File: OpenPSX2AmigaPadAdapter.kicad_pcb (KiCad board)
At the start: 2 copper layers, 58.9 x 44.2 mm, 43 parts, among them J1 TO_PSX_PAD, J2 DB9_F, J3 CONN_FTDI, J4 CONN_ICSP, J99 OSHW_LOGO, Q1 BSS138, Q2 BSS138, Q3 BSS138, Q4 BSS138, Q5 BSS138, U1 ATmega328P-AU, U2 LM1117-3.3, Y1 16M, Y2 16M

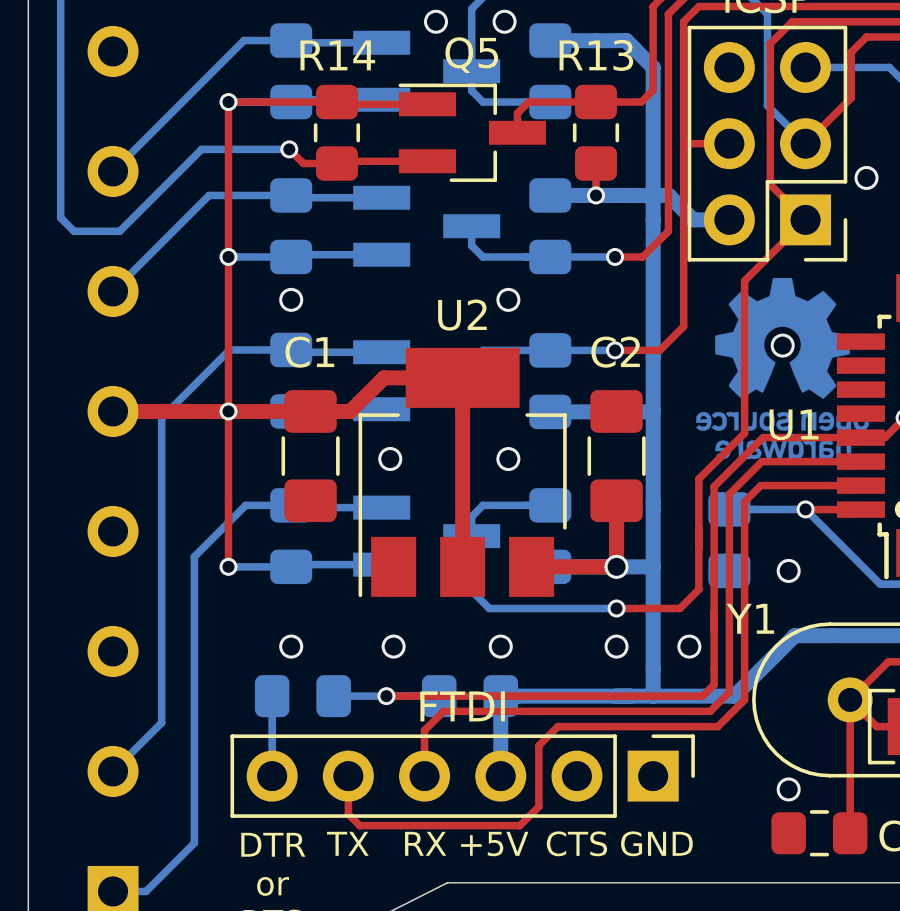
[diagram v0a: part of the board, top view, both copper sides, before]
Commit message: Update schematics for analog output support. PCB TBD.
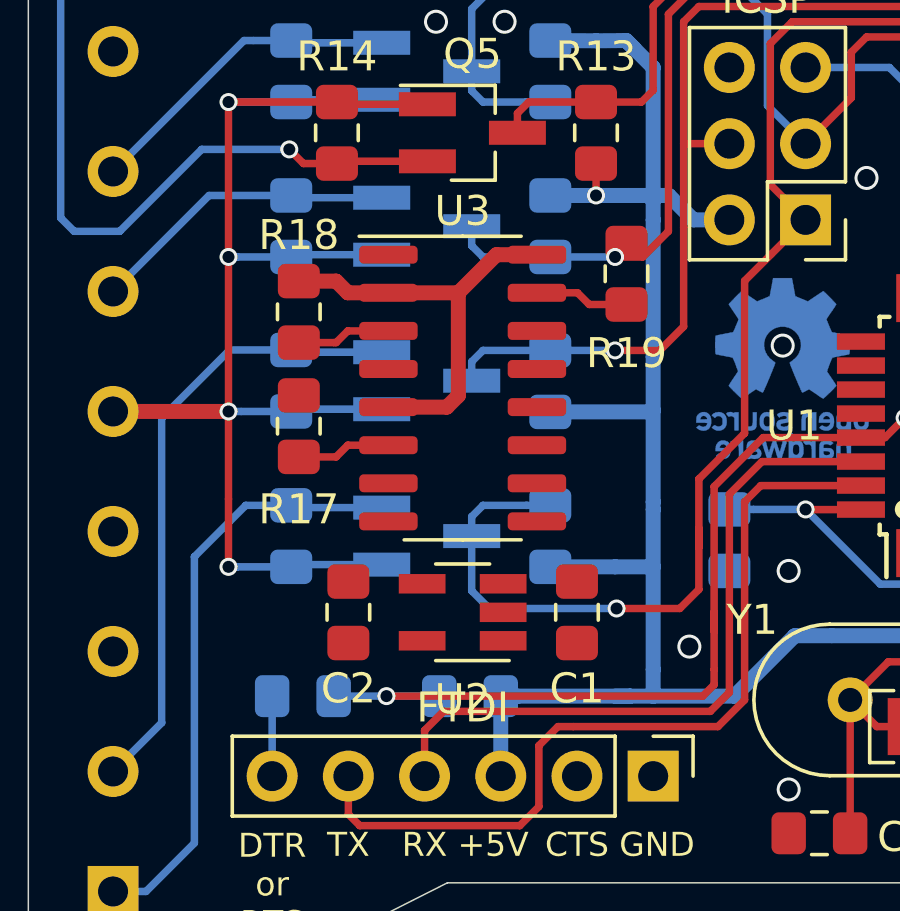
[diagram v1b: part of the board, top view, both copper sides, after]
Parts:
- added R17: 10k, Resistor_SMD:R_0805_2012Metric_Pad1.15x1.40mm_HandSolder, F.Cu at (122.8, 76.5)
- added R18: 1M, Resistor_SMD:R_0805_2012Metric_Pad1.15x1.40mm_HandSolder, F.Cu at (122.8, 72.7)
- added R19: 1M, Resistor_SMD:R_0805_2012Metric_Pad1.15x1.40mm_HandSolder, F.Cu at (133.7, 71.4)
- added U3: AD5242, Package_SO:SOIC-16_3.9x9.9mm_P1.27mm, F.Cu at (128.3, 75.2)
- C1, C2: value 10u -> 1u; footprint Capacitor_SMD:C_1206_3216Metric_Pad1.42x1.75mm_HandSolder -> Capacitor_SMD:C_0805_2012Metric_Pad1.15x1.40mm_HandSolder
- U2: value LM1117-3.3 -> TC1185-3.3V; footprint Package_TO_SOT_SMD:SOT-223-3_TabPin2 -> Package_TO_SOT_SMD:SOT-23-5_HandSoldering
- moved C2 10.3 mm to (124.5, 82.7), turned to 90 degrees
- moved C1 10.3 mm to (132.1, 82.7)
- moved U2 4.67 mm to (128.3, 82.7), turned to 180 degrees
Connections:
- C1 pad 1: GND -> +5V
- C1 pad 2: +3V3 -> GND
- C2 pad 1: GND -> +3V3
- C2 pad 2: +5V -> GND
- U1 pad 27: (no net) -> /sda
- U1 pad 28: (no net) -> /scl
- U2 pad 1: GND -> +5V
- U2 pad 2: +3V3 -> GND
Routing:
- net +3V3: track 61.2 -> 46.7 mm
- net +5V: track 106.1 -> 115.6 mm, vias 6 -> 5
- net Net-(R17-Pad1): track 0.00 -> 3.15 mm
- net /ami_potx: track 23.2 -> 26.3 mm
- net /ami_poty: track 18.2 -> 21.4 mm
- net GND: vias 42 -> 34

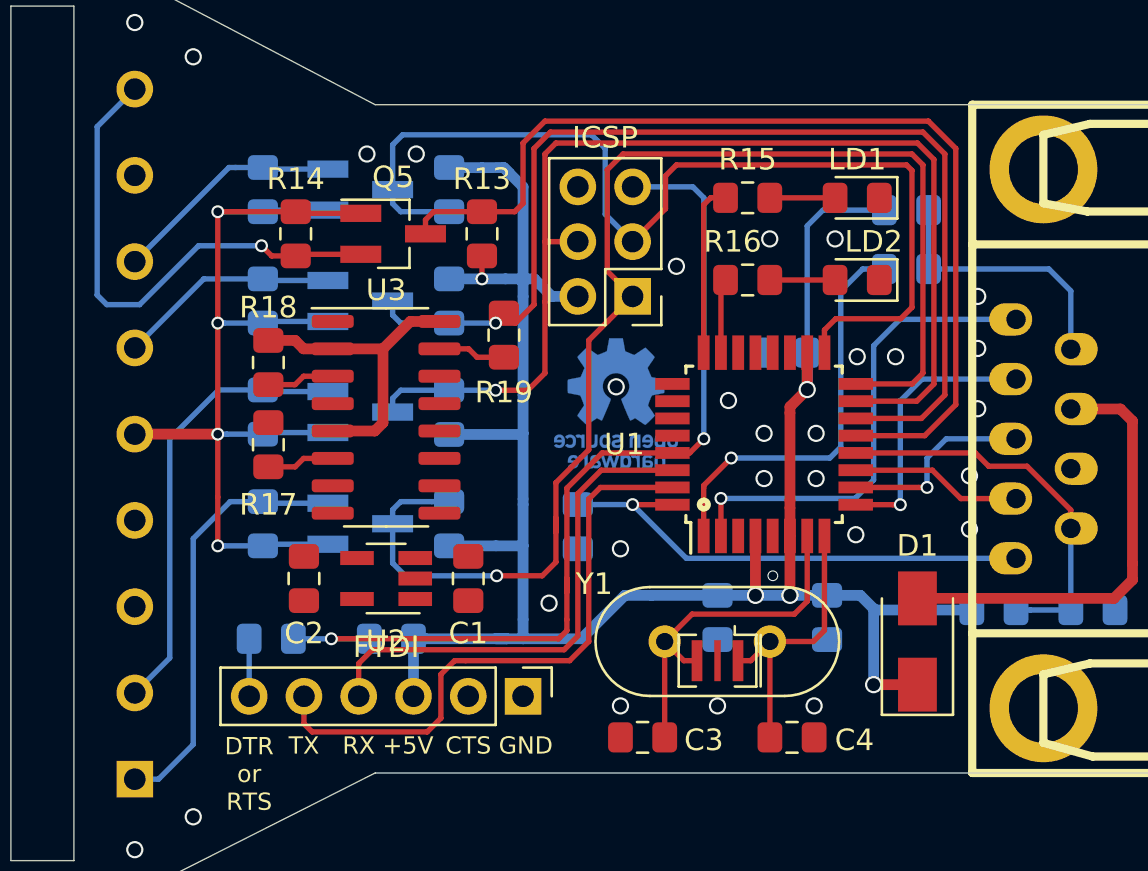
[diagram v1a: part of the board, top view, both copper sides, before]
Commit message: PCB modifications for analog support are complete
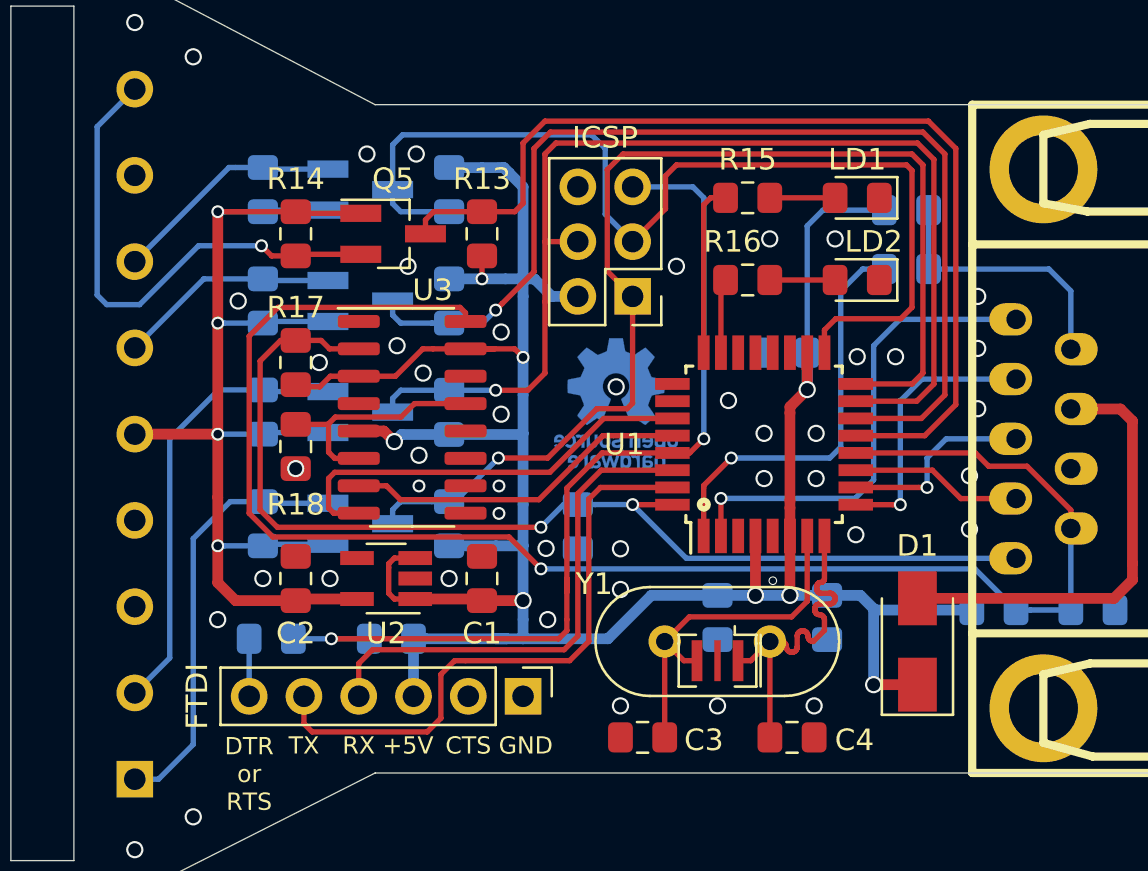
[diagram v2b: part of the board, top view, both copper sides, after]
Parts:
- removed R19: 1M, Resistor_SMD:R_0805_2012Metric_Pad1.15x1.40mm_HandSolder
- moved R18 1.27 mm to (124.1, 76.6), turned to 270 degrees
- moved R17 1.27 mm to (124.1, 72.7), turned to 270 degrees
- moved U3 1.21 mm to (129.5, 75.2)
- moved C1 0.63 mm to (132.7, 82.7)
- moved C2 0.38 mm to (124.1, 82.7)
- renumbered R18 to R17, R17 to R18
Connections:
- net Net-(C3-Pad2) renamed /clk-
- net Net-(C4-Pad2) renamed /clk+
- R18 pad 1: Net-(R17-Pad1) -> Net-(R18-Pad1)
- U3 pad 1: Net-(R17-Pad1) -> (no net)
- U3 pad 13: (no net) -> Net-(R18-Pad1)
- U3 pad 15: /ami_poty -> +5V
- U3 pad 16: +5V -> /ami_poty
- U3 pad 2: +5V -> /ami_potx
- U3 pad 3: /ami_potx -> +5V
- U3 pad 6: Net-(R17-Pad1) -> Net-(R18-Pad1)
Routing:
- net /ami_poty: track 21.4 -> 75.0 mm, vias 0 -> 1
- net /ami_potx: track 26.3 -> 50.7 mm, vias 1 -> 2
- net /sda: track 0.00 -> 20.0 mm
- net /scl: track 0.00 -> 16.0 mm
- net +5V: track 115.6 -> 127.6 mm, vias 5 -> 8
- net Net-(R18-Pad1): track 0.00 -> 11.1 mm
- net /miso: track 62.2 -> 53.3 mm
- net +3V3: track 46.7 -> 55.2 mm
- net /clk+: track 13.3 -> 16.5 mm
- net Net-(R17-Pad1): track 3.15 -> 0.00 mm
- net /ps_attn: track 50.5 -> 49.6 mm
- net GND: vias 34 -> 52

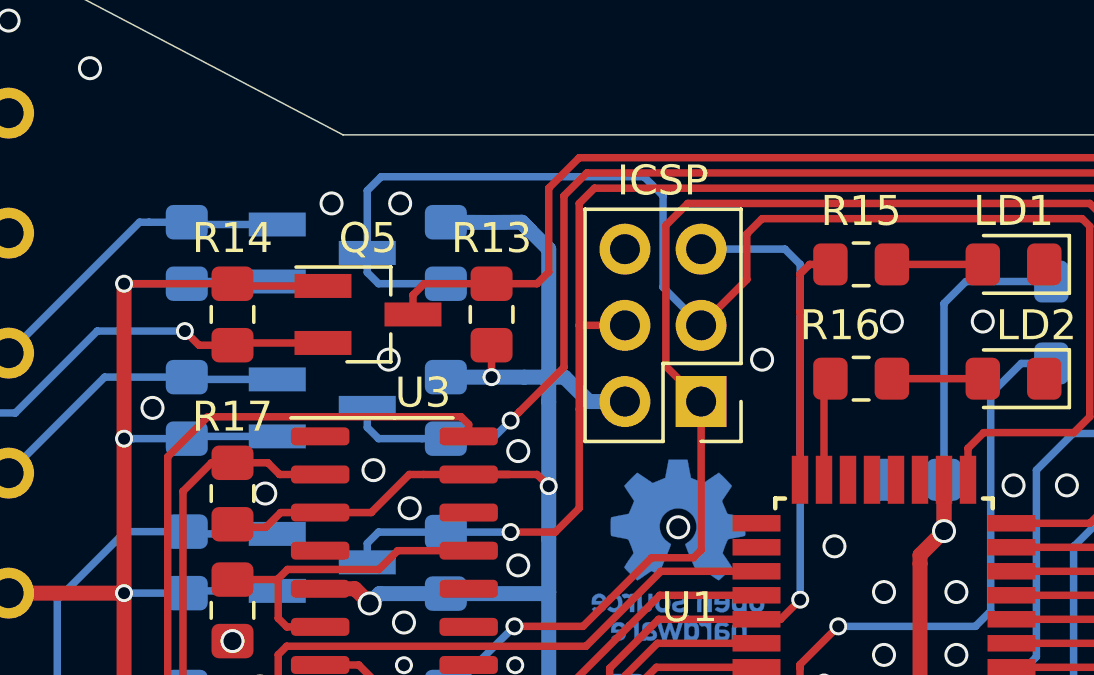
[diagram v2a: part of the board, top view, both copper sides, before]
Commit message: Fix component naming
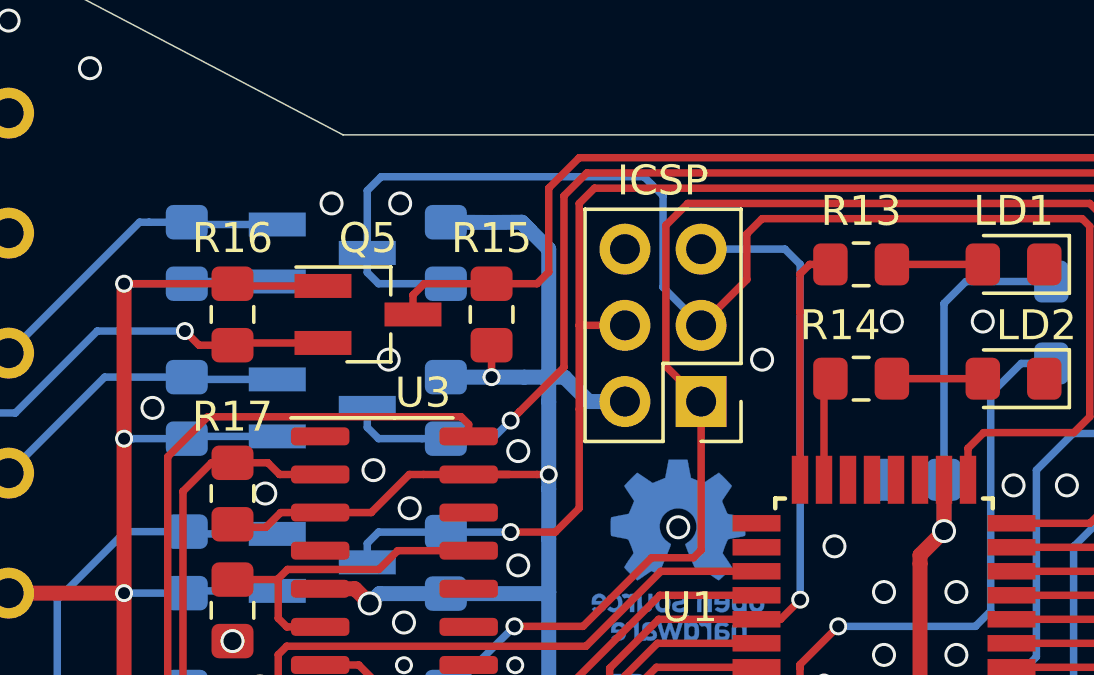
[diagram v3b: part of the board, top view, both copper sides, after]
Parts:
- renumbered R15 to R13, R16 to R14, R13 to R15, R14 to R16
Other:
- board text added: "V4"
- board text removed: "V3"
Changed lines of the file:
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@@
     (0 F.Cu signal)
     (31 B.Cu signal)
-    (36 B.SilkS user hide)
+    (36 B.SilkS user)
     (37 F.SilkS user)
     (38 B.Mask user)
@@
     (tags "resistor handsolder")
     (attr smd)
-    (fp_text reference R16 (at 0.6985 1.778) (layer F.SilkS)
+    (fp_text reference R14 (at 0.6985 1.778) (layer F.SilkS)
       (effects (font (size 1 1) (thickness 0.15)))
     )
@@
     (tags "resistor handsolder")
     (attr smd)
-    (fp_text reference R15 (at 0 1.778) (layer F.SilkS)
+    (fp_text reference R13 (at 0 1.778) (layer F.SilkS)
       (effects (font (size 1 1) (thickness 0.15)))
     )
@@
     (tags "resistor handsolder")
     (attr smd)
-    (fp_text reference R13 (at 2.542999 0 180) (layer F.SilkS)
+    (fp_text reference R15 (at 2.542999 0 180) (layer F.SilkS)
       (effects (font (size 1 1) (thickness 0.15)))
     )
@@
     (tags "resistor handsolder")
     (attr smd)
-    (fp_text reference R14 (at -2.542999 0 180) (layer F.SilkS)
+    (fp_text reference R16 (at -2.542999 0 180) (layer F.SilkS)
       (effects (font (size 1 1) (thickness 0.15)))
     )
@@
     (effects (font (size 1 1) (thickness 0.15)) (justify mirror))
   )
-  (gr_text V3 (at 165.862 90.424) (layer B.SilkS)
+  (gr_text V4 (at 165.862 90.424) (layer B.SilkS)
     (effects (font (size 1 1) (thickness 0.15)) (justify mirror))
   )
@@
   (segment (start 125.194502 73.787) (end 125.684501 73.297001) (width 0.25) (layer F.Cu) (net 2))
   (segment (start 133.304501 72.027001) (end 131.9515 72.027001) (width 0.25) (layer F.Cu) (net 2))
-  (via (at 134.62 72.417001) (size 0.6) (drill 0.4) (layers F.Cu B.Cu) (net 2))
+  (via (at 134.62 72.027001) (size 0.6) (drill 0.4) (layers F.Cu B.Cu) (net 2))
   (via (at 134.62 83.702) (size 0.8) (drill 0.6) (layers F.Cu B.Cu) (net 2))
   (segment (start 134.611 83.702) (end 134.62 83.693) (width 0.5) (layer F.Cu) (net 2))
@@
   (segment (start 128.161007 75.837001) (end 128.651006 76.327) (width 0.5) (layer F.Cu) (net 2))
   (segment (start 127.0015 75.837001) (end 128.161007 75.837001) (width 0.5) (layer F.Cu) (net 2))
-  (segment (start 134.23 72.027001) (end 134.62 72.417001) (width 0.25) (layer F.Cu) (net 2))
   (segment (start 131.9515 72.027001) (end 134.23 72.027001) (width 0.25) (layer F.Cu) (net 2))
   (segment (start 130.447001 72.027001) (end 131.9515 72.027001) (width 0.25) (layer F.Cu) (net 2))
@@
   (segment (start 128.702997 73.297001) (end 129.972997 72.027001) (width 0.25) (layer F.Cu) (net 2))
   (segment (start 127.0015 73.297001) (end 128.702997 73.297001) (width 0.25) (layer F.Cu) (net 2))
+  (segment (start 134.23 72.027001) (end 134.62 72.027001) (width 0.25) (layer F.Cu) (net 2))
   (via (at 120.4645 81.162) (size 0.6) (drill 0.4) (layers F.Cu B.Cu) (net 3))
   (segment (start 120.4645 78.9035) (end 120.4645 81.1165) (width 0.5) (layer F.Cu) (net 3))

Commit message: Ready for V4
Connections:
- net /dtr renamed /dtr_in
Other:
- board text added: "DTR or DTS"
- board text removed: "CTS"
- board text removed: "DTR or RTS"

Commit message: Make schematics clearer
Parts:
- R12: value 10k -> 1M
- turned R12 to 180 degrees
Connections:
- R12 pad 1: +5V -> /ami_poty
- R12 pad 2: /ami_poty -> +5V
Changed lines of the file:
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@@
   )
   (module Resistor_SMD:R_0805_2012Metric_Pad1.15x1.40mm_HandSolder (layer B.Cu)
-    (at 156.455 84.1375)
+    (at 156.455 84.1375 180)
     (descr "Resistor SMD 0805 (2012 Metric), square (rectangular) end terminal, IPC_7351 nominal with elongated pad for handsoldering. (Body size source: https://docs.google.com/spreadsheets/d/1BsfQQcO9C6DZCsRaXUlFlo91Tg2WpOkGARC1WS5S8t0/edit?usp=sharing), generated with kicad-footprint-generator")
     (tags "resistor handsolder")
     (attr smd)
-    (fp_text reference R12 (at -3.547 0.0635) (layer B.SilkS)
+    (fp_text reference R12 (at 3.547 -0.0635) (layer B.SilkS)
       (effects (font (size 1 1) (thickness 0.15)) (justify mirror))
     )
-    (fp_text value 10k (at 0 -1.65) (layer B.Fab)
+    (fp_text value 1M (at 0 -1.65) (layer B.Fab)
       (effects (font (size 1 1) (thickness 0.15)) (justify mirror))
     )
@@
       (effects (font (size 0.5 0.5) (thickness 0.08)) (justify mirror))
     )
-    (pad 1 smd roundrect (at -1.025 0) (size 1.15 1.4) (layers B.Cu B.Paste B.Mask) (roundrect_rratio 0.217391)
+    (pad 1 smd roundrect (at -1.025 0 180) (size 1.15 1.4) (layers B.Cu B.Paste B.Mask) (roundrect_rratio 0.217391)
+      (net 15 /ami_poty))
+    (pad 2 smd roundrect (at 1.025 0 180) (size 1.15 1.4) (layers B.Cu B.Paste B.Mask) (roundrect_rratio 0.217391)
       (net 2 +5V))
-    (pad 2 smd roundrect (at 1.025 0) (size 1.15 1.4) (layers B.Cu B.Paste B.Mask) (roundrect_rratio 0.217391)
-      (net 15 /ami_poty))
     (model ${KISYS3DMOD}/Resistor_SMD.3dshapes/R_0805_2012Metric.wrl
       (at (xyz 0 0 0))
@@
   (segment (start 125.5715 75.9075) (end 122.63 75.9075) (width 0.25) (layer B.Cu) (net 3) (status 30))
   (segment (start 122.63 75.9075) (end 122.555 75.9825) (width 0.25) (layer B.Cu) (net 3) (status 30))
-  (segment (start 121.92 85.471) (end 121.92 88.138) (width 0.25) (layer B.Cu) (net 35) (status 30))
   (via (at 143.002 76.2) (size 0.6) (drill 0.4) (layers F.Cu B.Cu) (net 4))
   (segment (start 141.546 76.854) (end 142.348 76.854) (width 0.25) (layer F.Cu) (net 4) (status 10))
@@
   (segment (start 125.603 76.820202) (end 125.889799 77.107001) (width 0.25) (layer F.Cu) (net 34))
   (segment (start 125.603 75.5015) (end 125.603 76.820202) (width 0.25) (layer F.Cu) (net 34))
+  (segment (start 121.92 85.471) (end 121.92 88.138) (width 0.25) (layer B.Cu) (net 35) (status 30))
   (zone (net 1) (net_name GND) (layer F.Cu) (hatch edge 0.508)
     (connect_pads (clearance 0.1))
